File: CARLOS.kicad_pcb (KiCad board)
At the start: 2 copper layers, 57.5 x 61 mm, 6 parts, among them J1 PH, J2 Conductividad, J3 Humedad, J4 BME280, J5 BH1750, U1 Heltec_ESP32_LoRa_V3

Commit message: hola
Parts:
- moved J3 5.72 mm to (66.4, 29.3)
- moved J2 3.21 mm to (59.6, 29.2)
- moved J1 3.13 mm to (54.7, 29.8)
- moved J5 2.45 mm to (49.6, 29.3)
- turned U1 to 180 degrees
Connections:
- U1 pad J3_1: unconnected-(U1B-GND_J3-PadJ3_1) -> GND
- U1 pad J3_2: 3V3 -> +3.3V
- U1 pad J3_3: 3V3 -> +3.3V

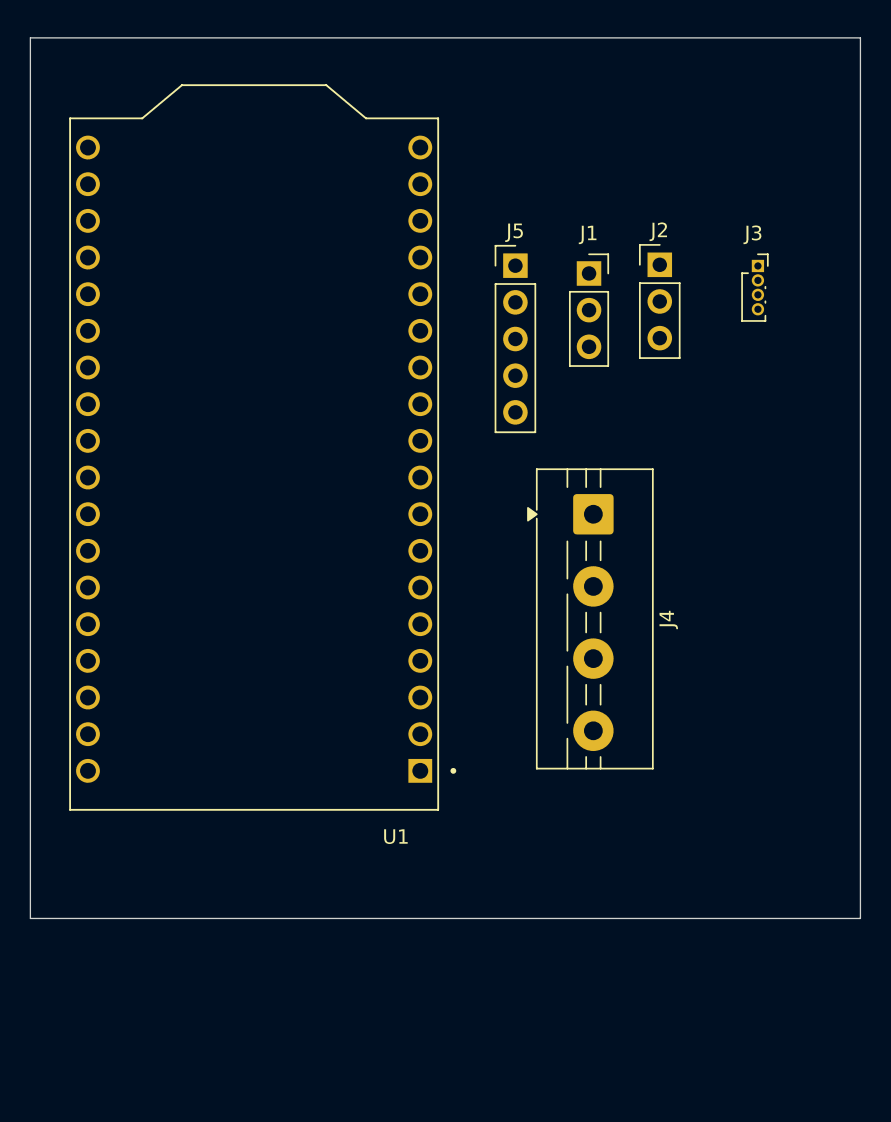
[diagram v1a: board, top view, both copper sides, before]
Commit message: PCB Finalizado
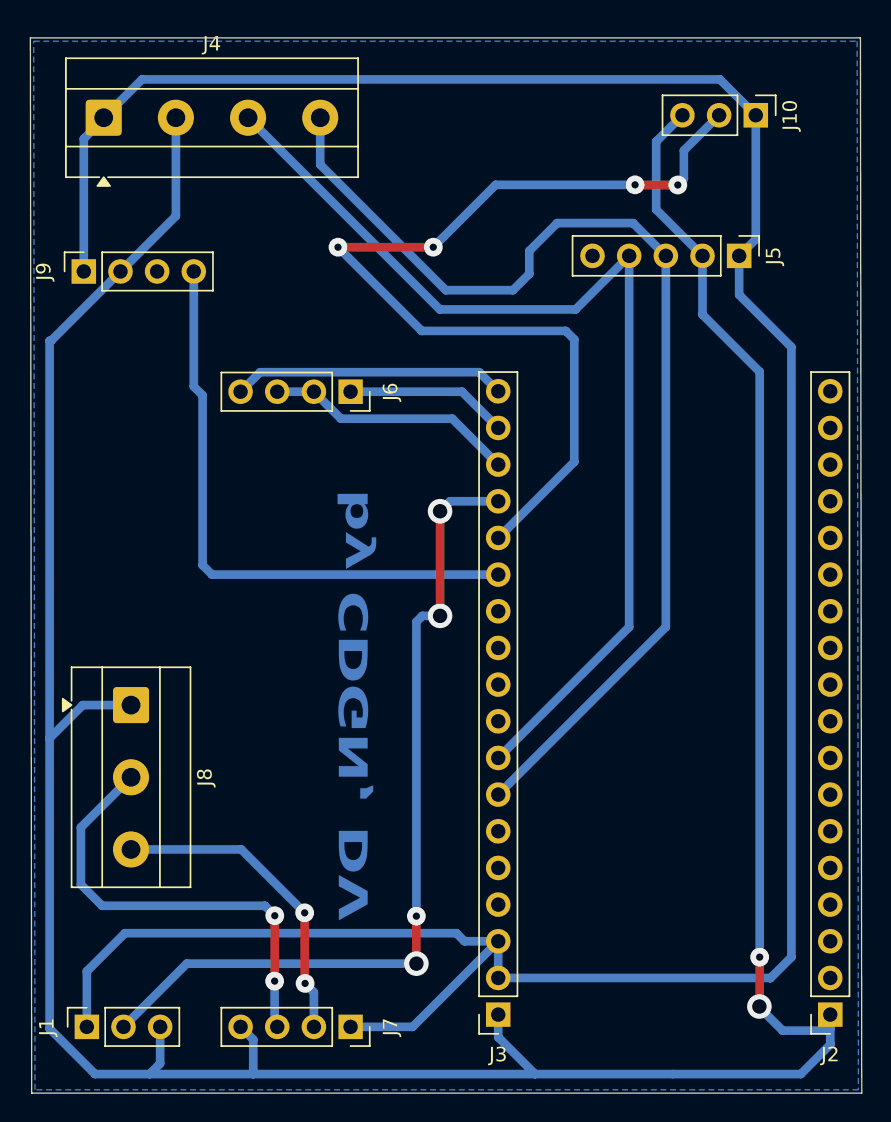
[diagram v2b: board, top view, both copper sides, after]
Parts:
- removed U1: Heltec_ESP32_LoRa_V3, Heltec_ESP32_LoRa_V3:Heltec_ESP32_LoRa_V3
- added J2: DER, Connector_PinSocket_2.54mm:PinSocket_1x18_P2.54mm_Vertical, F.Cu at (71.4, 81.2)
- added J3: IZQ, Connector_PinSocket_2.54mm:PinSocket_1x18_P2.54mm_Vertical, F.Cu at (48.4, 81.2)
- added J6: Max485 to Micro, Connector_PinSocket_2.54mm:PinSocket_1x04_P2.54mm_Vertical, F.Cu at (38.2, 38.0)
- added J7: VCC to Max485, Connector_PinSocket_2.54mm:PinSocket_1x04_P2.54mm_Vertical, F.Cu at (38.2, 82.0)
- added J8: NPK, TerminalBlock_MetzConnect:TerminalBlock_MetzConnect_Type055_RT01503HDWU_1x03_P5.00mm_Horizontal, F.Cu at (23.0, 59.7)
- J4: footprint TerminalBlock:TerminalBlock_MaiXu_MX126-5.0-04P_1x04_P5.00mm -> TerminalBlock_MetzConnect:TerminalBlock_MetzConnect_Type055_RT01504HDWU_1x04_P5.00mm_Horizontal
- J9: renamed from J3; footprint Connector_PinSocket_1.00mm:PinSocket_1x04_P1.00mm_Vertical -> Connector_PinSocket_2.54mm:PinSocket_1x04_P2.54mm_Vertical
- moved J1 62.7 mm to (19.9, 82.0), turned to 90 degrees
- moved J9 46.7 mm to (19.7, 29.7), turned to 90 degrees
- moved J4 43.6 mm to (21.1, 19.0), turned to 0 degrees
- moved J5 15.5 mm to (65.1, 28.6), turned to -90 degrees
- moved J10 12.3 mm to (66.2, 18.9), turned to -90 degrees
- renumbered J2 to J10
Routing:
- net GND: track 0.00 -> 215.3 mm, vias 0 -> 2
- net +3.3V: track 0.00 -> 188.6 mm
- net /GPIO42: track 0.00 -> 76.7 mm
- net /GPIO41: track 0.00 -> 72.0 mm
- net /GPIO3: track 0.00 -> 66.3 mm, vias 0 -> 4
- net /GPIO4: track 0.00 -> 59.2 mm, vias 0 -> 4
- net /GPIO2: track 0.00 -> 41.4 mm
- net /A: track 0.00 -> 31.0 mm, vias 0 -> 2
- net /B: track 0.00 -> 22.0 mm, vias 0 -> 2
- net /GPIO7: track 0.00 -> 19.0 mm
- net /GPIO5: track 0.00 -> 17.4 mm
- net /GPIO6: track 0.00 -> 11.3 mm
- added copper zone on B.Cu, net GND
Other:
- board size 57.5 x 61 mm -> 57.6 x 73.1 mm
- board text added: "by CDGN, DV"
